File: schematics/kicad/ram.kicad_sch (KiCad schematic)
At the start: 32 parts, among them U1200 HM53461, U1201 HM53461, U1202 HM53461, U1203 HM53461, U1204 HM53461, U1205 HM53461, U1206 HM53461, U1207 HM53461, U1208 HM53461, U1209 HM53461, U1210 HM53461, U1211 HM53461, U1212 HM53461, U1213 HM53461, U1214 HM53461, U1215 HM53461, U1216 HM53461, U1217 HM53461, U1218 HM53461, U1219 HM53461, U1220 HM53461, U1221 HM53461, U1222 HM53461, U1223 HM53461, U1224 HM53461, U1225 HM53461, U1226 HM53461, U1227 HM53461, U1228 HM53461, U1229 HM53461, U1230 HM53461, U1231 HM53461

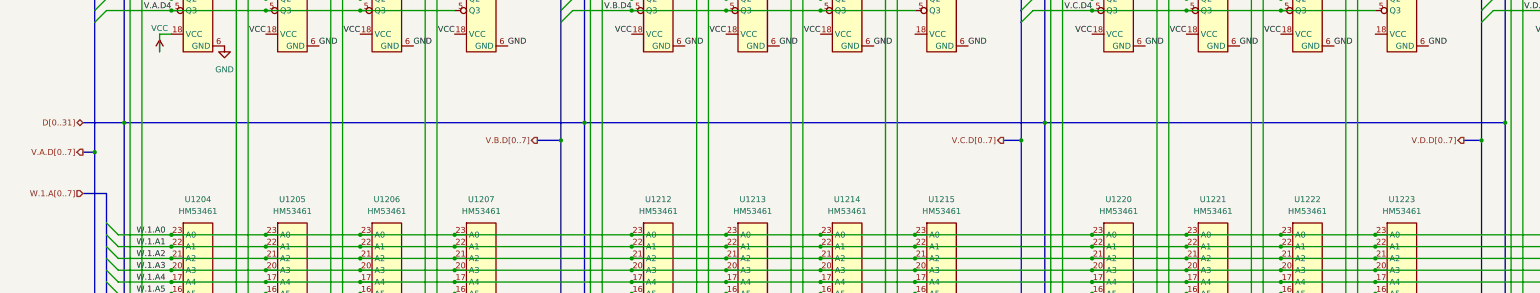
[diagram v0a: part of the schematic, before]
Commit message: Fill in more output section
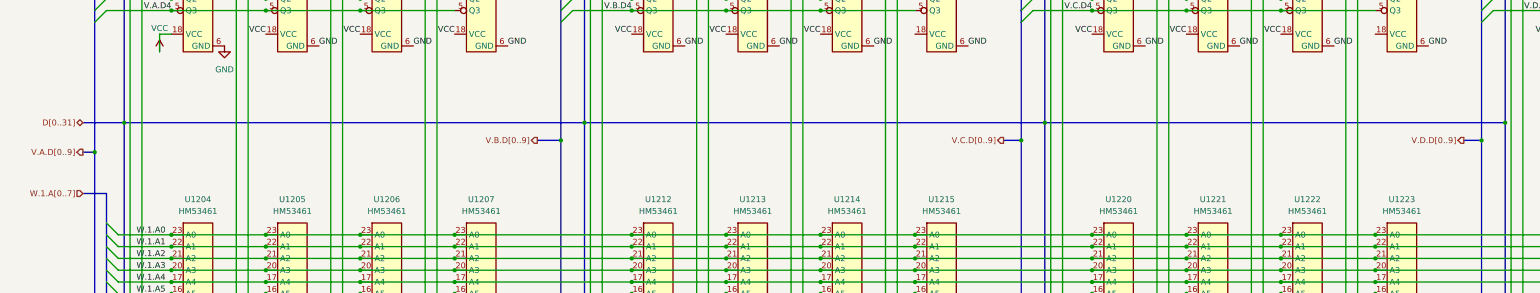
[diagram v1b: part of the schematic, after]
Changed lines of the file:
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@@
 		)
 	)
-	(hierarchical_label "V.C.D[0..7]"
+	(hierarchical_label "V.C.D[0..9]"
 		(shape output)
 		(at 223.52 125.73 180)
@@
 		)
 	)
-	(hierarchical_label "V.D.D[0..7]"
+	(hierarchical_label "V.D.D[0..9]"
 		(shape output)
 		(at 322.58 125.73 180)
@@
 		)
 	)
-	(hierarchical_label "V.B.D[0..7]"
+	(hierarchical_label "V.B.D[0..9]"
 		(shape output)
 		(at 123.19 125.73 180)
@@
 		)
 	)
-	(hierarchical_label "V.A.D[0..7]"
+	(hierarchical_label "V.A.D[0..9]"
 		(shape output)
 		(at 25.4 128.27 180)

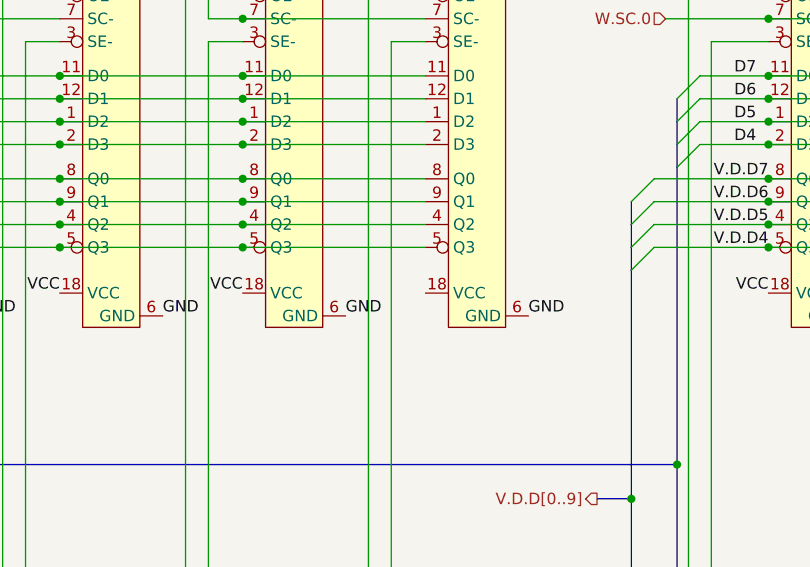
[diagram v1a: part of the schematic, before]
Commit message: First initial layout, fix ZIP footprint.
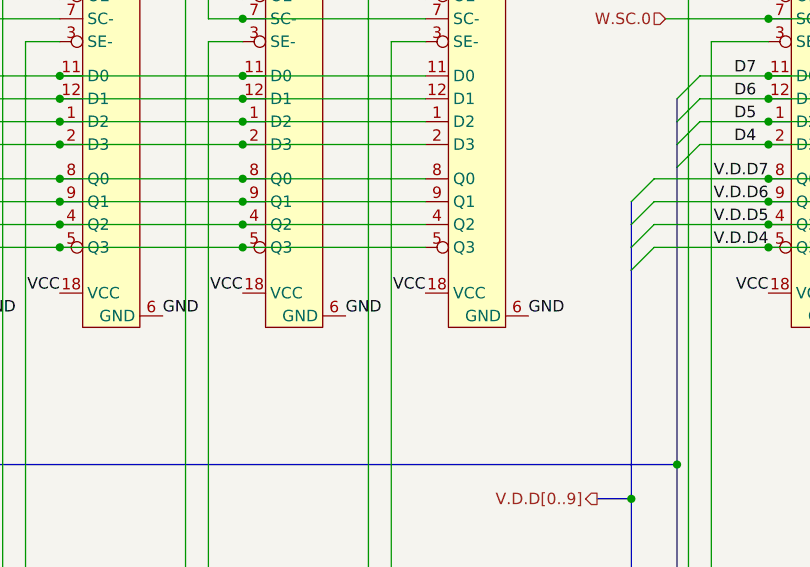
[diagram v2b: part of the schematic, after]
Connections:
- net VCC: now also U1219.18 (VCC)
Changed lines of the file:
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@@
+		)
+	)
+	(label "VCC"
+		(at 303.53 102.87 180)
+		(effects
+			(font
+				(size 1.27 1.27)
+			)
+			(justify right bottom)
 		)
 	)

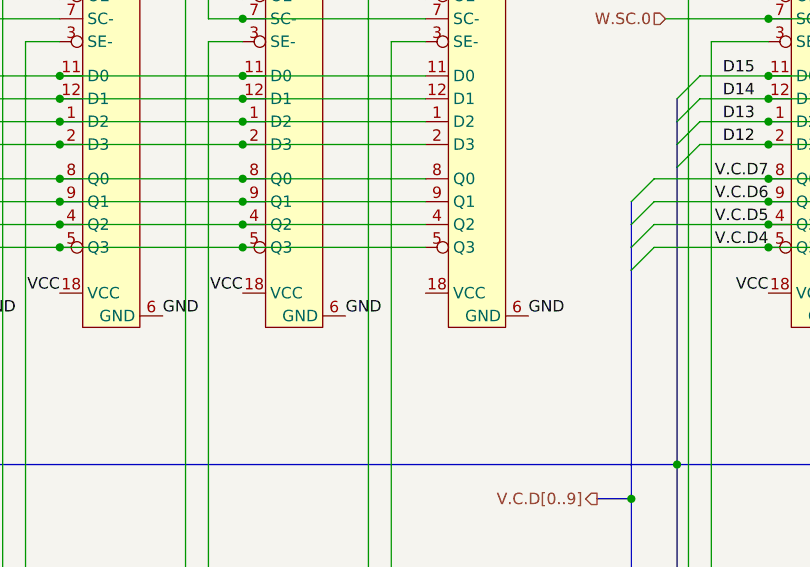
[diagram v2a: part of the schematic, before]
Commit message: Fix layout of the memory chips based on the board Fix the orientation of the P4 connector Connect CS.DAC- based on the board Change the orientation of the ECL resistors to route better Fix the copper islands to match the board, only DAC is on analog island, ECL and crystal are separate. Fix ECL VCC to VCC Confirm VEE not used Add PALs - U1000 missing
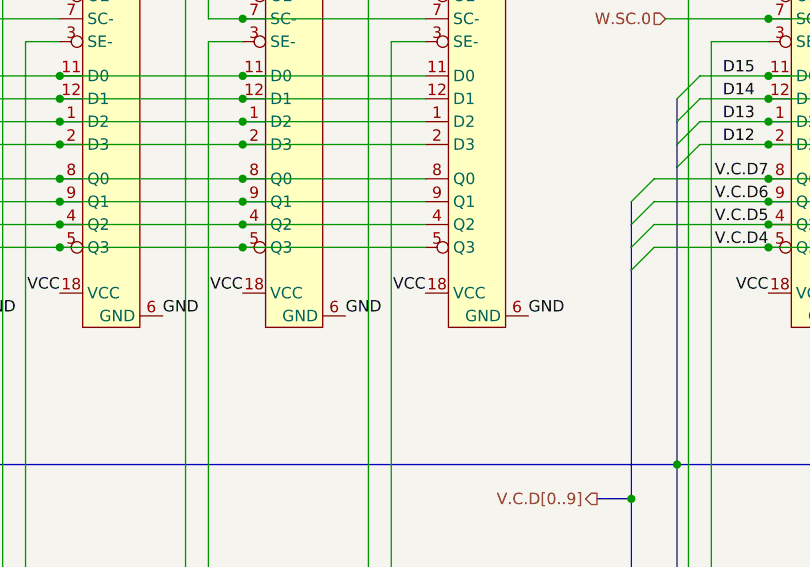
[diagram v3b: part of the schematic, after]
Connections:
- net VCC: now also U1211.18 (VCC)
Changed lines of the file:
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@@
+		)
+	)
+	(label "VCC"
+		(at 204.47 102.87 180)
+		(effects
+			(font
+				(size 1.27 1.27)
+			)
+			(justify right bottom)
 		)
 	)

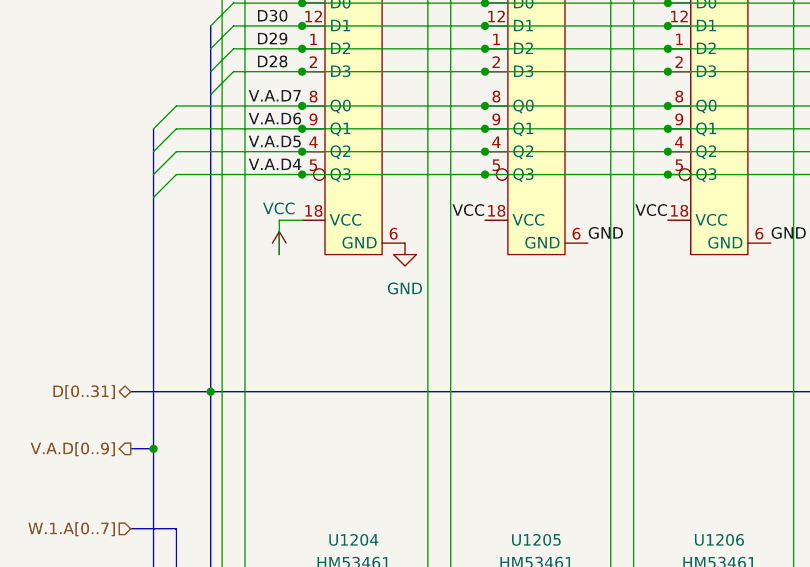
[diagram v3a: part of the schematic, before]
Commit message: Fix ERCs which uncovered some issues with W.RE for the overlay memory. Finish the ECL chips for clock control - need to find value of R1315. Add space for 0-ohm resistor on V.VSYN which exists in schematics but was never connected in the original composite sync scheme with 4 BNC connectors. Can leave it unconnected if it causes issues.
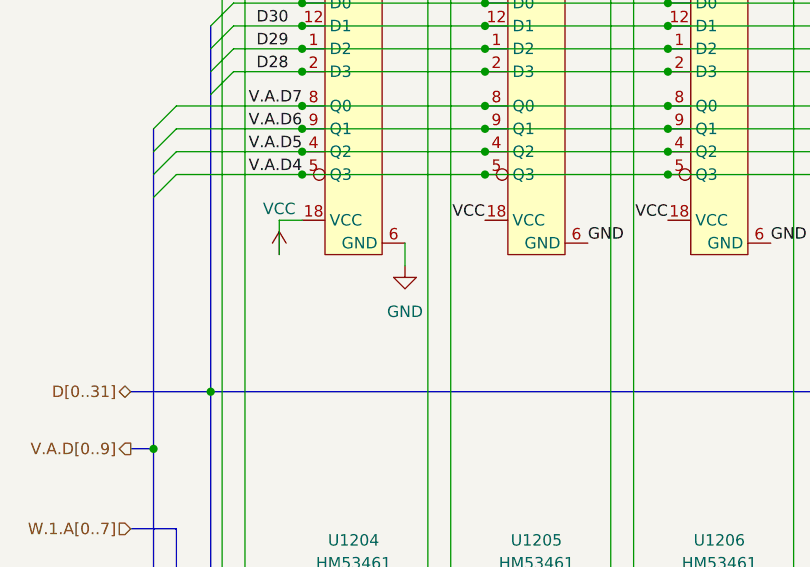
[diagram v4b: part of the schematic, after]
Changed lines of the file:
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@@
 		)
 	)
+	(wire
+		(pts
+			(xy 55.88 107.95) (xy 55.88 105.41)
+		)
+		(stroke
+			(width 0)
+			(type default)
+		)
+	)
 	(bus
 		(pts
@@
 	)
 	(symbol
+		(lib_id "power:GND")
+		(at 55.88 107.95 0)
+		(unit 1)
+		(exclude_from_sim no)
+		(in_bom yes)
+		(on_board yes)
+		(dnp no)
+		(fields_autoplaced yes)
+		(property "Reference" "#PWR02"
+			(at 55.88 114.3 0)
+			(effects
+				(font
+					(size 1.27 1.27)
+				)
+				(hide yes)
+			)
+		)
+		(property "Value" "GND"
+			(at 55.88 113.03 0)
+			(effects
+				(font
+					(size 1.27 1.27)
+				)
+			)
+		)
+		(property "Footprint" ""
+			(at 55.88 107.95 0)
+			(effects
+				(font
+					(size 1.27 1.27)
+				)
+				(hide yes)
+			)
+		)
+		(property "Datasheet" ""
+			(at 55.88 107.95 0)
+			(effects
+				(font
+					(size 1.27 1.27)
+				)
+				(hide yes)
+			)
+		)
+		(property "Description" "Power symbol creates a global label with name \"GND\" , ground"
+			(at 55.88 107.95 0)
+			(effects
+				(font
+					(size 1.27 1.27)
+				)
+				(hide yes)
+			)
+		)
+		(pin "1"
+		)
+		(instances
+			(project "cg4"
+				(path "/7c2b6a13-c303-4adb-8eed-6e6a9ac5307e/c18d90d3-c0ca-466c-a85b-7325eebe578d"
+					(reference "#PWR02")
+					(unit 1)
+				)
+			)
+		)
+	)
+	(symbol
 		(lib_id "cg4:HM53461")
 		(at 110.49 36.83 0)
@@
 					(unit 1)
 				)
-			)
-		)
-	)
-	(symbol
-		(lib_id "power:GND")
-		(at 55.88 105.41 0)
-		(unit 1)
-		(exclude_from_sim no)
-		(in_bom yes)
-		(on_board yes)
-		(dnp no)
-		(fields_autoplaced yes)
-		(property "Reference" "#PWR02"
-			(at 55.88 111.76 0)
-			(effects
-				(font
-					(size 1.27 1.27)
-				)
-				(hide yes)
-			)
-		)
-		(property "Value" "GND"
-			(at 55.88 110.49 0)
-			(effects
-				(font
-					(size 1.27 1.27)
-				)
-			)
-		)
-		(property "Footprint" ""
-			(at 55.88 105.41 0)
-			(effects
-				(font
-					(size 1.27 1.27)
-				)
-				(hide yes)
-			)
-		)
-		(property "Datasheet" ""
-			(at 55.88 105.41 0)
-			(effects
-				(font
-					(size 1.27 1.27)
-				)
-				(hide yes)
-			)
-		)
-		(property "Description" "Power symbol creates a global label with name \"GND\" , ground"
-			(at 55.88 105.41 0)
-			(effects
-				(font
-					(size 1.27 1.27)
-				)
-				(hide yes)
-			)
-		)
-		(pin "1"
-		)
-		(instances
-			(project ""
-				(path "/7c2b6a13-c303-4adb-8eed-6e6a9ac5307e/c18d90d3-c0ca-466c-a85b-7325eebe578d"
-					(reference "#PWR02")
-					(unit 1)
-				)

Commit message: Finish routing and misc fixes in the analog section
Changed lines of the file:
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@@
 	(wire
 		(pts
-			(xy 41.91 106.68) (xy 41.91 102.87)
+			(xy 41.91 104.14) (xy 41.91 102.87)
 		)
 		(stroke
@@
 	(symbol
 		(lib_id "power:VCC")
-		(at 41.91 106.68 0)
+		(at 41.91 104.14 0)
 		(unit 1)
 		(exclude_from_sim no)
@@
 		(fields_autoplaced yes)
 		(property "Reference" "#PWR01"
-			(at 41.91 110.49 0)
+			(at 41.91 107.95 0)
 			(effects
 				(font
@@
 		)
 		(property "Value" "VCC"
-			(at 41.91 101.6 0)
+			(at 41.91 99.06 0)
 			(effects
 				(font
@@
 		)
 		(property "Footprint" ""
-			(at 41.91 106.68 0)
+			(at 41.91 104.14 0)
 			(effects
 				(font
@@
 		)
 		(property "Datasheet" ""
-			(at 41.91 106.68 0)
+			(at 41.91 104.14 0)
 			(effects
 				(font
@@
 		)
 		(property "Description" "Power symbol creates a global label with name \"VCC\""
-			(at 41.91 106.68 0)
+			(at 41.91 104.14 0)
 			(effects
 				(font
